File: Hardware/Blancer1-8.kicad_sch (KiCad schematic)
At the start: 28 parts, among them Q36 PMXB360ENEA, Q37 2SA1832, Q38 IRLU120NPBF, Q39 BSS84AKW, Q40 BSS84AKW, U12 TLV9052

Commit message: generate BOM
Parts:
- C46: value 100n -> DNP
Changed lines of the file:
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@@
       (effects (font (size 1.27 1.27)) (justify right))
     )
-    (property "Value" "100n" (id 1) (at 107.95 133.3499 0)
+    (property "Value" "DNP" (id 1) (at 107.95 133.3499 0)
       (effects (font (size 1.27 1.27)) (justify right))
     )

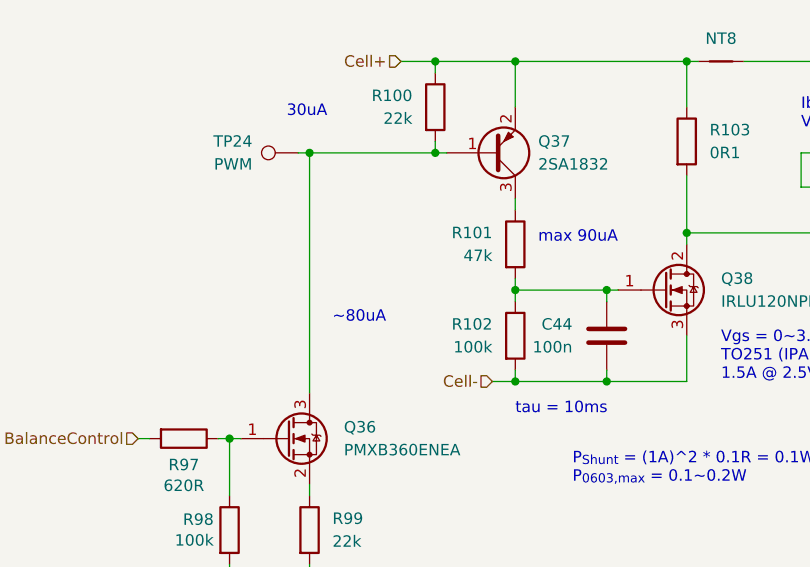
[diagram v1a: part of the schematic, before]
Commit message: hardware: update to KiCad 7
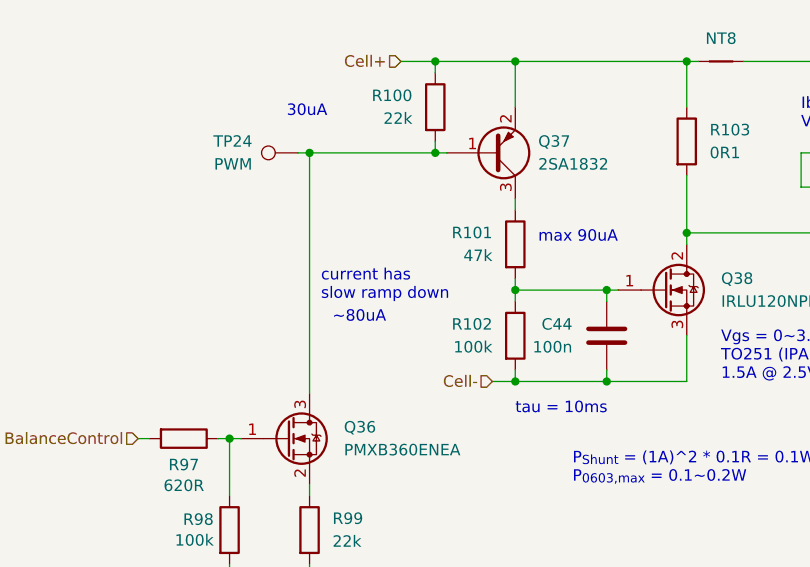
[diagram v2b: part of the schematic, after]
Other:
- note added: "current has slow ramp down"

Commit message: hardware: version 1
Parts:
- removed Q36: PMXB360ENEA, 0_ProjectLibrary:DFN1010-3, symbol Device:Q_NMOS_GSD
- removed Q37: 2SA1832, Package_TO_SOT_SMD:SOT-416, symbol Device:Q_PNP_BEC
- removed R100, R99: 22k, Resistor_SMD:R_0402_1005Metric, symbol Device:R
- removed R101: 47k, Resistor_SMD:R_0402_1005Metric, symbol Device:R
- removed R97: 620R, Resistor_SMD:R_0402_1005Metric, symbol Device:R
- removed R98: 100k, Resistor_SMD:R_0402_1005Metric, symbol Device:R
- added C50: 3.3n, Capacitor_SMD:C_0402_1005Metric, symbol Device:C
- added D11, D19, D27: RB751S40, Diode_SMD:D_SOD-523, symbol Device:D
- added D3: BZT52H-C6V2, Diode_SMD:D_SOD-123F, symbol Device:D_Zener
- added R119, R135: 620R, Resistor_SMD:R_0402_1005Metric, symbol Device:R
- added R127: 22k, Resistor_SMD:R_0402_1005Metric, symbol Device:R
- C14: renamed from C44; Mfr. Part# (none) -> GRM155R71C104KA88D; Mouser Part# (none) -> 81-GRM155R71C104KA88
- C15: renamed from C45; Mfr. Part# (none) -> GRM155R71C104KA88D; Mouser Part# (none) -> 81-GRM155R71C104KA88
- C16: renamed from C46; value DNP -> 100n; Mfr. Part# (none) -> GRM155R71C104KA88D; Mouser Part# (none) -> 81-GRM155R71C104KA88
- C17: renamed from C47; Mfr. Part# (none) -> GRM155R71C104KA88D; Mouser Part# (none) -> 81-GRM155R71C104KA88
- C18: renamed from C48; Mfr. Part# (none) -> GRM155R71C104KA88D; Mouser Part# (none) -> 81-GRM155R71C104KA88
- Q10: renamed from Q40; Mfr. Part# (none) -> BSS84AKW,115; Mouser Part# (none) -> 771-BSS84AKW115
- Q8: renamed from Q38; Mfr. Part# (none) -> IRLU120NPBF; Mouser Part# (none) -> 942-IRLU120NPBF
- Q9: renamed from Q39; Mfr. Part# (none) -> BSS84AKW,115; Mouser Part# (none) -> 771-BSS84AKW115
- R24: renamed from R102; value 100k -> 330k; Mfr. Part# (none) -> RC0402FR-0722KL; Mouser Part# (none) -> 603-RC0402FR-0722KL
- R25: renamed from R103; Mfr. Part# (none) -> PT0603FR-7W0R1L; Mouser Part# (none) -> 603-PT0603FR-7W0R1L
- R26: renamed from R104; Mfr. Part# (none) -> RC0402FR-134K7L; Mouser Part# (none) -> 603-RC0402FR-134K7L
- R27: renamed from R105; Mfr. Part# (none) -> RC0402FR-0722KL; Mouser Part# (none) -> 603-RC0402FR-0722KL
- R28: renamed from R106; Mfr. Part# (none) -> RC0402FR-134K7L; Mouser Part# (none) -> 603-RC0402FR-134K7L
- R29: renamed from R107; Mfr. Part# (none) -> RC0402FR-134K7L; Mouser Part# (none) -> 603-RC0402FR-134K7L
- R30: renamed from R108; Mfr. Part# (none) -> RC0402FR-07620RL; Mouser Part# (none) -> 603-RC0402FR-07620RL
- R31: renamed from R109; Mfr. Part# (none) -> RC0402FR-134K7L; Mouser Part# (none) -> 603-RC0402FR-134K7L
- U6: renamed from U12; Mfr. Part# (none) -> TLV9052IDDFR; Mouser Part# (none) -> 595-TLV9052IDDFR
- renumbered NT8 to NT2, TP24 to TP6, TP25 to TP7, TP26 to TP8
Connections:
- net BalanceControl: now also C50.1
- net Cell+: now also C16.1, D27.1 (K), D3.1 (K)
- net Cell-: now also D19.2 (A), D3.2 (A); no longer C16.2
- net at C14.1, Q8.1 (G), R24.1: now also D11.1 (K), D27.2 (A)
- net at Q8.2 (D), R25.2: now also R119.1; no longer U6.5 (+)
- net at TP6.1: now also C50.2, R127.1, R135.2
- net at R26.1, R27.1, U6.3 (+): now also C16.2; no longer C16.1
- new net: D19.1 (K), R135.1
- new net: R119.2, U6.5 (+)
- new net: D11.2 (A), R127.2
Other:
- note removed: "30uA"
- note removed: "P_{FET,max} = 35V * 80uA = 2.8mW"
- note removed: "current has slow ramp down"
- note removed: "max 90uA"
- note removed: "~80uA"
- moved on the sheet: C16, TP6
